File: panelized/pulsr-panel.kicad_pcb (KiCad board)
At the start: 2 copper layers, 99 x 94.5 mm, 243 parts, among them J1 JST_PH, J2 0.1" header, Q1 FDN339AN

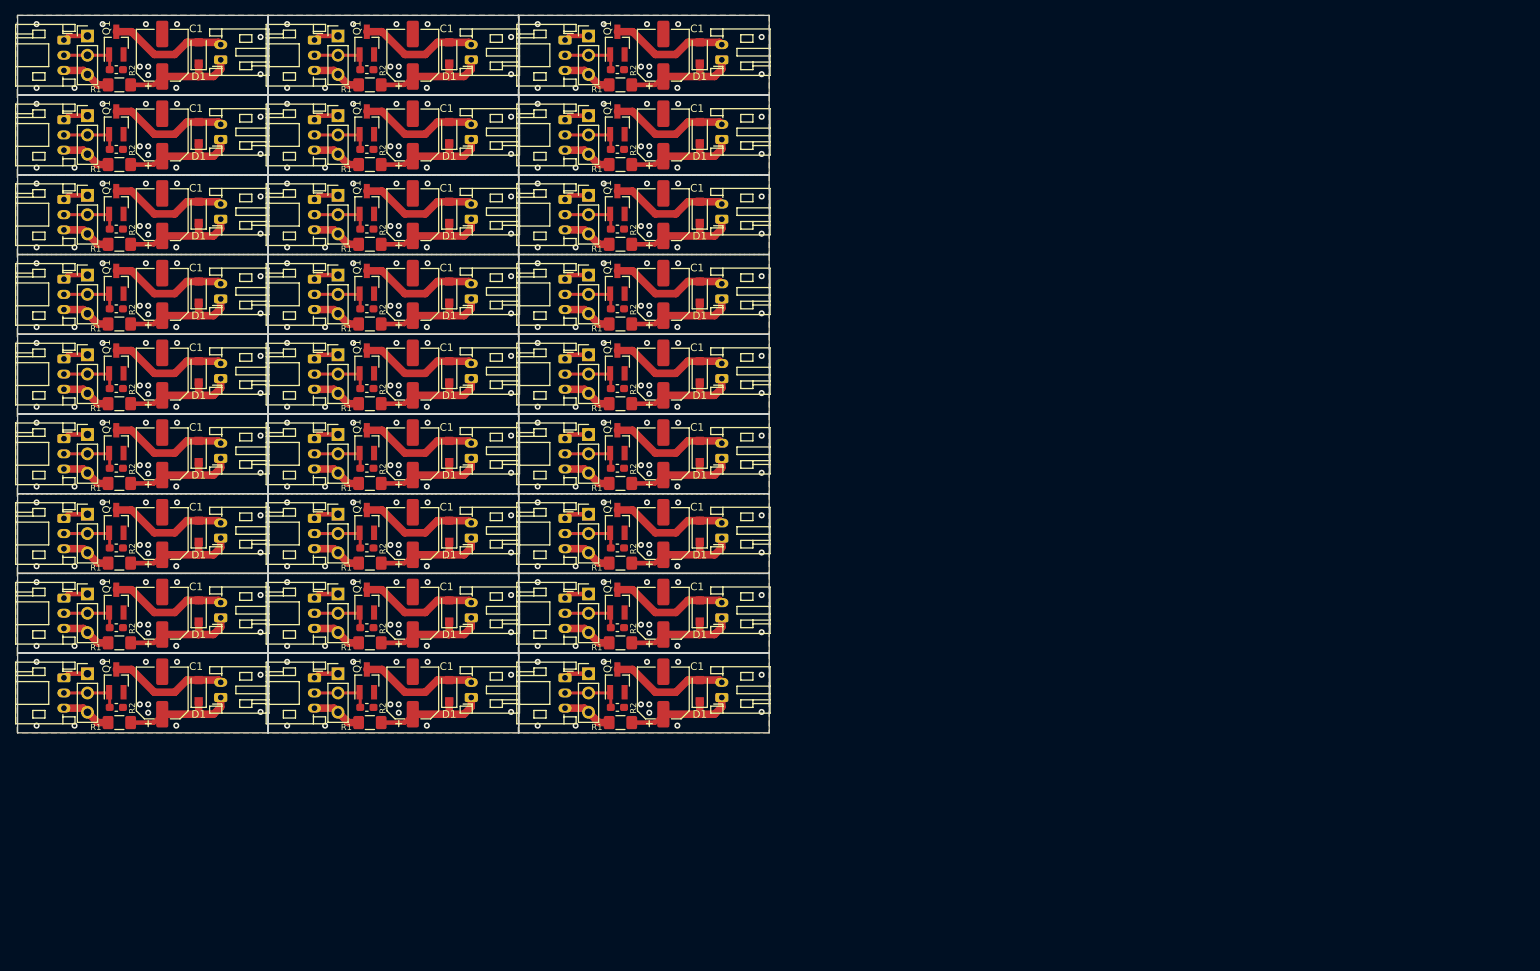
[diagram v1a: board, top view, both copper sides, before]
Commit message: Modified design to fit 47mF super-cap
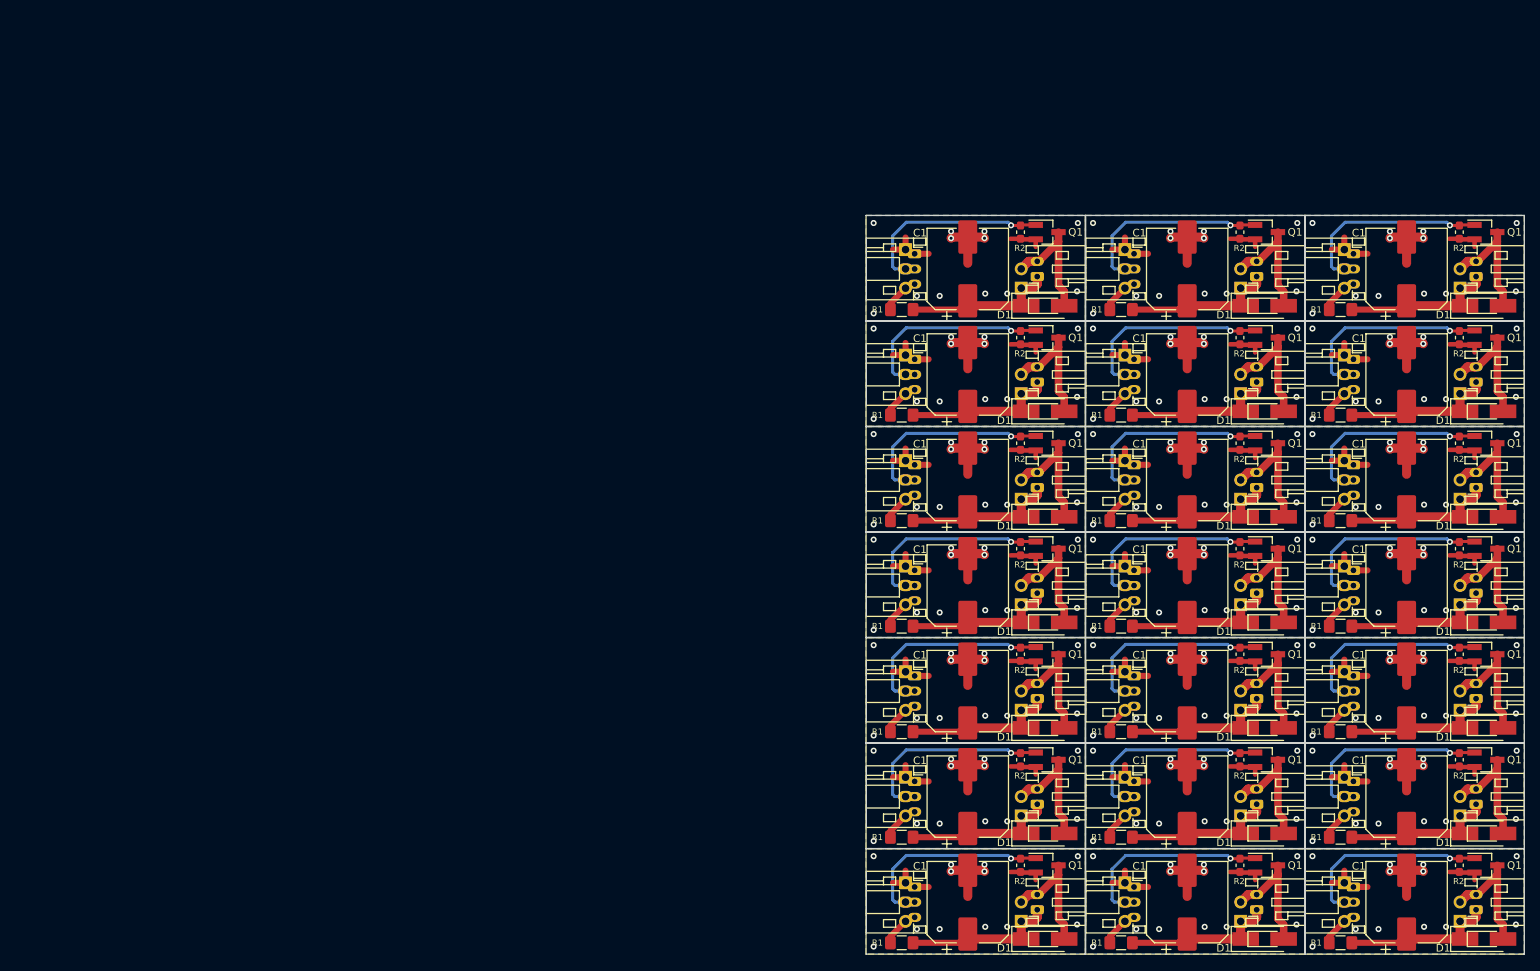
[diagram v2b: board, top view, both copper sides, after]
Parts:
- removed the C1 at (105.6, 109.6)
- removed the C1 at (105.6, 78.1)
- removed the C1 at (72.6, 78.1)
- removed the C1 at (39.6, 78.1)
- removed the C1 at (105.6, 67.6)
- removed the C1 at (72.6, 67.6)
- removed the C1 at (39.6, 67.6)
- removed the C1 at (105.6, 57.1)
- removed the C1 at (72.6, 57.1)
- removed the C1 at (39.6, 57.1)
- removed the C1 at (105.6, 46.6)
- removed the C1 at (72.6, 109.6)
- removed the C1 at (72.6, 46.6)
- removed the C1 at (39.6, 46.6)
- removed the C1 at (105.6, 36.1)
- removed the C1 at (72.6, 36.1)
- removed the C1 at (39.6, 36.1)
- removed the C1 at (105.6, 25.6)
- removed the C1 at (72.6, 25.6)
- removed the C1 at (39.6, 25.6)
- removed the C1 at (39.6, 109.6)
- removed the C1 at (105.6, 99.1)
- removed the C1 at (72.6, 99.1)
- removed the C1 at (39.6, 99.1)
- removed the C1 at (105.6, 88.6)
- removed the C1 at (72.6, 88.6)
- removed the C1 at (39.6, 88.6)
- removed the D1 at (110.4, 109.3)
- removed the D1 at (110.4, 77.8)
- removed the D1 at (77.4, 77.8)
- removed the D1 at (44.4, 77.8)
- removed the D1 at (110.4, 67.3)
- removed the D1 at (77.4, 67.3)
- removed the D1 at (44.4, 67.3)
- removed the D1 at (110.4, 56.8)
- removed the D1 at (77.4, 56.8)
- removed the D1 at (44.4, 56.8)
- removed the D1 at (110.4, 46.3)
- removed the D1 at (77.4, 109.3)
- removed the D1 at (77.4, 46.3)
- removed the D1 at (44.4, 46.3)
- removed the D1 at (110.4, 35.8)
- removed the D1 at (77.4, 35.8)
- removed the D1 at (44.4, 35.8)
- removed the D1 at (110.4, 25.3)
- removed the D1 at (77.4, 25.3)
- removed the D1 at (44.4, 109.3)
- removed the D1 at (110.4, 98.8)
- removed the D1 at (77.4, 98.8)
- removed the D1 at (44.4, 98.8)
- removed the D1 at (110.4, 88.3)
- removed the D1 at (77.4, 88.3)
- removed the D1 at (44.4, 88.3)
- removed the G*** at (104.3, 110.1)
- removed the G*** at (104.3, 78.6)
- removed the G*** at (71.3, 78.6)
- removed the G*** at (38.3, 78.6)
- removed the G*** at (104.3, 68.1)
- removed the G*** at (71.3, 68.1)
- removed the G*** at (38.3, 68.1)
- removed the G*** at (104.3, 57.6)
- removed the G*** at (71.3, 57.6)
- removed the G*** at (38.3, 57.6)
- removed the G*** at (104.3, 47.1)
- removed the G*** at (71.3, 110.1)
- removed the G*** at (71.3, 47.1)
- removed the G*** at (38.3, 47.1)
- removed the G*** at (104.3, 36.6)
- removed the G*** at (71.3, 36.6)
- removed the G*** at (38.3, 36.6)
- removed the G*** at (104.3, 26.1)
- removed the G*** at (71.3, 26.1)
- removed the G*** at (38.3, 26.1)
- removed the G*** at (38.3, 110.1)
- removed the G*** at (104.3, 99.6)
- removed the G*** at (71.3, 99.6)
- removed the G*** at (38.3, 99.6)
- removed the G*** at (104.3, 89.1)
- removed the G*** at (71.3, 89.1)
- removed the G*** at (38.3, 89.1)
- removed the J1 at (92.7, 107.6)
- removed the J1 at (92.7, 76.1)
- removed the J1 at (59.6, 76.1)
- removed the J1 at (26.6, 76.1)
- removed the J1 at (92.7, 65.6)
- removed the J1 at (59.6, 65.6)
- removed the J1 at (26.6, 65.6)
- removed the J1 at (92.7, 55.1)
- removed the J1 at (59.6, 55.1)
- removed the J1 at (26.6, 55.1)
- removed the J1 at (92.7, 44.6)
- removed the J1 at (59.6, 107.6)
- removed the J1 at (59.6, 44.6)
- removed the J1 at (26.6, 44.6)
- removed the J1 at (92.7, 34.1)
- removed the J1 at (59.6, 34.1)
- removed the J1 at (26.6, 34.1)
- removed the J1 at (92.7, 23.6)
- removed the J1 at (59.6, 23.6)
- removed the J1 at (26.6, 23.6)
- removed the J1 at (26.6, 107.6)
- removed the J1 at (92.7, 97.1)
- removed the J1 at (59.6, 97.1)
- removed the J1 at (26.6, 97.1)
- removed the J1 at (92.7, 86.6)
- removed the J1 at (59.6, 86.6)
- removed the J1 at (26.6, 86.6)
- removed the J2 at (95.8, 107.1)
- removed the J2 at (95.8, 75.6)
- removed the J2 at (62.8, 75.6)
- removed the J2 at (29.8, 75.6)
- removed the J2 at (95.8, 65.1)
- removed the J2 at (62.8, 65.1)
- removed the J2 at (29.8, 65.1)
- removed the J2 at (95.8, 54.6)
- removed the J2 at (62.8, 54.6)
- removed the J2 at (29.8, 54.6)
- removed the J2 at (95.8, 44.1)
- removed the J2 at (62.8, 107.1)
- removed the J2 at (62.8, 44.1)
- removed the J2 at (29.8, 44.1)
- removed the J2 at (95.8, 33.6)
- removed the J2 at (62.8, 33.6)
- removed the J2 at (29.8, 33.6)
- removed the J2 at (95.8, 23.1)
- removed the J2 at (62.8, 23.1)
- removed the J2 at (29.8, 107.1)
- removed the J2 at (95.8, 96.6)
- removed the J2 at (62.8, 96.6)
- removed the J2 at (29.8, 96.6)
- removed the J2 at (95.8, 86.1)
- removed the J2 at (62.8, 86.1)
- removed the J2 at (29.8, 86.1)
- removed the L1 at (113.3, 110.2)
- removed the L1 at (113.3, 78.7)
- removed the L1 at (80.3, 78.7)
- removed the L1 at (47.3, 78.7)
- removed the L1 at (113.3, 68.2)
- removed the L1 at (80.3, 68.2)
- removed the L1 at (47.3, 68.2)
- removed the L1 at (113.3, 57.7)
- removed the L1 at (80.3, 57.7)
- removed the L1 at (47.3, 57.7)
- removed the L1 at (113.3, 47.2)
- removed the L1 at (80.3, 110.2)
- removed the L1 at (80.3, 47.2)
- removed the L1 at (47.3, 47.2)
- removed the L1 at (113.3, 36.7)
- removed the L1 at (80.3, 36.7)
- removed the L1 at (47.3, 36.7)
- removed the L1 at (113.3, 26.2)
- removed the L1 at (80.3, 26.2)
- removed the L1 at (47.3, 26.2)
- removed the L1 at (47.3, 110.2)
- removed the L1 at (113.3, 99.7)
- removed the L1 at (80.3, 99.7)
- removed the L1 at (47.3, 99.7)
- removed the L1 at (113.3, 89.2)
- removed the L1 at (80.3, 89.2)
- removed the L1 at (47.3, 89.2)
- removed the Q1 at (99.5, 108.0)
- removed the Q1 at (99.5, 76.5)
- removed the Q1 at (66.5, 76.5)
- removed the Q1 at (33.5, 76.5)
- removed the Q1 at (99.5, 66.0)
- removed the Q1 at (66.5, 66.0)
- removed the Q1 at (33.5, 66.0)
- removed the Q1 at (99.5, 55.5)
- removed the Q1 at (66.5, 55.5)
- removed the Q1 at (33.5, 55.5)
- removed the Q1 at (99.5, 45.0)
- removed the Q1 at (66.5, 108.0)
- removed the Q1 at (66.5, 45.0)
- removed the Q1 at (33.5, 45.0)
- removed the Q1 at (99.5, 34.5)
- removed the Q1 at (66.5, 34.5)
- removed the Q1 at (33.5, 34.5)
- removed the Q1 at (99.5, 24.0)
- removed the Q1 at (66.5, 24.0)
- removed the Q1 at (33.5, 108.0)
- removed the Q1 at (99.5, 97.5)
- removed the Q1 at (66.5, 97.5)
- removed the Q1 at (33.5, 97.5)
- removed the Q1 at (99.5, 87.0)
- removed the Q1 at (66.5, 87.0)
- removed the Q1 at (33.5, 87.0)
- removed the R1 at (100.0, 113.5)
- removed the R1 at (100.0, 82.0)
- removed the R1 at (67.0, 82.0)
- removed the R1 at (34.0, 82.0)
- removed the R1 at (100.0, 71.5)
- removed the R1 at (67.0, 71.5)
- removed the R1 at (34.0, 71.5)
- removed the R1 at (100.0, 61.0)
- removed the R1 at (67.0, 61.0)
- removed the R1 at (34.0, 61.0)
- removed the R1 at (100.0, 50.5)
- removed the R1 at (67.0, 113.5)
- removed the R1 at (67.0, 50.5)
- removed the R1 at (34.0, 50.5)
- removed the R1 at (100.0, 40.0)
- removed the R1 at (67.0, 40.0)
- removed the R1 at (34.0, 40.0)
- removed the R1 at (100.0, 29.5)
- removed the R1 at (67.0, 29.5)
- removed the R1 at (34.0, 113.5)
- removed the R1 at (100.0, 103.0)
- removed the R1 at (67.0, 103.0)
- removed the R1 at (34.0, 103.0)
- removed the R1 at (100.0, 92.5)
- removed the R1 at (67.0, 92.5)
- removed the R1 at (34.0, 92.5)
- removed the R2 at (99.5, 111.5)
- removed the R2 at (99.5, 80.0)
- removed the R2 at (66.5, 80.0)
- removed the R2 at (33.5, 80.0)
- removed the R2 at (99.5, 69.5)
- removed the R2 at (66.5, 69.5)
- removed the R2 at (33.5, 69.5)
- removed the R2 at (99.5, 59.0)
- removed the R2 at (66.5, 59.0)
- removed the R2 at (33.5, 59.0)
- removed the R2 at (99.5, 48.5)
- removed the R2 at (66.5, 111.5)
- removed the R2 at (66.5, 48.5)
- removed the R2 at (33.5, 48.5)
- removed the R2 at (99.5, 38.0)
- removed the R2 at (66.5, 38.0)
- removed the R2 at (33.5, 38.0)
- removed the R2 at (99.5, 27.5)
- removed the R2 at (66.5, 27.5)
- removed the R2 at (33.5, 111.5)
- removed the R2 at (99.5, 101.0)
- removed the R2 at (66.5, 101.0)
- removed the R2 at (33.5, 101.0)
- removed the R2 at (99.5, 90.5)
- removed the R2 at (66.5, 90.5)
- removed the R2 at (33.5, 90.5)
- added C1: FC0H473ZFTBR24, Capacitor_SMD:CP_Elec_10x10.5, F.Cu at (145.7, 53.8)
- added C1: FC0H473ZFTBR24, Capacitor_SMD:CP_Elec_10x10.5, F.Cu at (145.7, 95.5)
- added C1: FC0H473ZFTBR24, Capacitor_SMD:CP_Elec_10x10.5, F.Cu at (174.6, 95.5)
- added C1: FC0H473ZFTBR24, Capacitor_SMD:CP_Elec_10x10.5, F.Cu at (203.5, 95.5)
- added C1: FC0H473ZFTBR24, Capacitor_SMD:CP_Elec_10x10.5, F.Cu at (145.7, 109.3)
- added C1: FC0H473ZFTBR24, Capacitor_SMD:CP_Elec_10x10.5, F.Cu at (174.6, 109.3)
- added C1: FC0H473ZFTBR24, Capacitor_SMD:CP_Elec_10x10.5, F.Cu at (203.5, 109.3)
- added C1: FC0H473ZFTBR24, Capacitor_SMD:CP_Elec_10x10.5, F.Cu at (145.7, 123.2)
- added C1: FC0H473ZFTBR24, Capacitor_SMD:CP_Elec_10x10.5, F.Cu at (174.6, 123.2)
- added C1: FC0H473ZFTBR24, Capacitor_SMD:CP_Elec_10x10.5, F.Cu at (203.5, 123.2)
- added C1: FC0H473ZFTBR24, Capacitor_SMD:CP_Elec_10x10.5, F.Cu at (145.7, 137.2)
- added C1: FC0H473ZFTBR24, Capacitor_SMD:CP_Elec_10x10.5, F.Cu at (174.6, 53.8)
- added C1: FC0H473ZFTBR24, Capacitor_SMD:CP_Elec_10x10.5, F.Cu at (174.6, 137.2)
- added C1: FC0H473ZFTBR24, Capacitor_SMD:CP_Elec_10x10.5, F.Cu at (203.5, 137.2)
- added C1: FC0H473ZFTBR24, Capacitor_SMD:CP_Elec_10x10.5, F.Cu at (203.5, 53.8)
- added C1: FC0H473ZFTBR24, Capacitor_SMD:CP_Elec_10x10.5, F.Cu at (145.7, 67.7)
- added C1: FC0H473ZFTBR24, Capacitor_SMD:CP_Elec_10x10.5, F.Cu at (174.6, 67.7)
- added C1: FC0H473ZFTBR24, Capacitor_SMD:CP_Elec_10x10.5, F.Cu at (203.5, 67.7)
- added C1: FC0H473ZFTBR24, Capacitor_SMD:CP_Elec_10x10.5, F.Cu at (145.7, 81.5)
- added C1: FC0H473ZFTBR24, Capacitor_SMD:CP_Elec_10x10.5, F.Cu at (174.6, 81.5)
- added C1: FC0H473ZFTBR24, Capacitor_SMD:CP_Elec_10x10.5, F.Cu at (203.5, 81.5)
- added D1: 1N4007L, Diode_SMD:D_SOD-123F, F.Cu at (155.9, 58.6)
- added D1: 1N4007L, Diode_SMD:D_SOD-123F, F.Cu at (155.9, 100.3)
- added D1: 1N4007L, Diode_SMD:D_SOD-123F, F.Cu at (184.8, 100.3)
- added D1: 1N4007L, Diode_SMD:D_SOD-123F, F.Cu at (213.7, 100.3)
- added D1: 1N4007L, Diode_SMD:D_SOD-123F, F.Cu at (155.9, 114.2)
- added D1: 1N4007L, Diode_SMD:D_SOD-123F, F.Cu at (184.8, 114.2)
- added D1: 1N4007L, Diode_SMD:D_SOD-123F, F.Cu at (213.7, 114.2)
- added D1: 1N4007L, Diode_SMD:D_SOD-123F, F.Cu at (155.9, 128.1)
- added D1: 1N4007L, Diode_SMD:D_SOD-123F, F.Cu at (184.8, 128.1)
- added D1: 1N4007L, Diode_SMD:D_SOD-123F, F.Cu at (213.7, 128.1)
- added D1: 1N4007L, Diode_SMD:D_SOD-123F, F.Cu at (155.9, 142.0)
- added D1: 1N4007L, Diode_SMD:D_SOD-123F, F.Cu at (184.8, 58.6)
- added D1: 1N4007L, Diode_SMD:D_SOD-123F, F.Cu at (184.8, 142.0)
- added D1: 1N4007L, Diode_SMD:D_SMA_Handsoldering, F.Cu at (155.9, 58.6)
- added D1: 1N4007L, Diode_SMD:D_SMA_Handsoldering, F.Cu at (184.8, 58.6)
- added D1: 1N4007L, Diode_SMD:D_SMA_Handsoldering, F.Cu at (213.7, 58.6)
- added D1: 1N4007L, Diode_SMD:D_SMA_Handsoldering, F.Cu at (155.9, 72.5)
- added D1: 1N4007L, Diode_SMD:D_SMA_Handsoldering, F.Cu at (184.8, 72.5)
- added D1: 1N4007L, Diode_SMD:D_SMA_Handsoldering, F.Cu at (213.7, 72.5)
- added D1: 1N4007L, Diode_SMD:D_SMA_Handsoldering, F.Cu at (155.9, 86.4)
- added D1: 1N4007L, Diode_SMD:D_SMA_Handsoldering, F.Cu at (184.8, 86.4)
- added D1: 1N4007L, Diode_SMD:D_SMA_Handsoldering, F.Cu at (213.7, 86.4)
- added D1: 1N4007L, Diode_SMD:D_SOD-123F, F.Cu at (213.7, 58.6)
- added D1: 1N4007L, Diode_SMD:D_SMA_Handsoldering, F.Cu at (155.9, 100.3)
- added D1: 1N4007L, Diode_SMD:D_SMA_Handsoldering, F.Cu at (184.8, 100.3)
- added D1: 1N4007L, Diode_SMD:D_SMA_Handsoldering, F.Cu at (213.7, 100.3)
- added D1: 1N4007L, Diode_SMD:D_SMA_Handsoldering, F.Cu at (155.9, 114.2)
- added D1: 1N4007L, Diode_SMD:D_SMA_Handsoldering, F.Cu at (184.8, 114.2)
- added D1: 1N4007L, Diode_SMD:D_SMA_Handsoldering, F.Cu at (213.7, 114.2)
- added D1: 1N4007L, Diode_SMD:D_SMA_Handsoldering, F.Cu at (155.9, 128.1)
- added D1: 1N4007L, Diode_SMD:D_SMA_Handsoldering, F.Cu at (184.8, 128.1)
- added D1: 1N4007L, Diode_SMD:D_SMA_Handsoldering, F.Cu at (213.7, 128.1)
- added D1: 1N4007L, Diode_SMD:D_SMA_Handsoldering, F.Cu at (155.9, 142.0)
- added D1: 1N4007L, Diode_SMD:D_SOD-123F, F.Cu at (155.9, 72.5)
- added D1: 1N4007L, Diode_SMD:D_SMA_Handsoldering, F.Cu at (184.8, 142.0)
- added D1: 1N4007L, Diode_SMD:D_SMA_Handsoldering, F.Cu at (213.7, 142.0)
- added D1: 1N4007L, Diode_SMD:D_SOD-123F, F.Cu at (184.8, 72.5)
- added D1: 1N4007L, Diode_SMD:D_SOD-123F, F.Cu at (213.7, 72.5)
- added D1: 1N4007L, Diode_SMD:D_SOD-123F, F.Cu at (155.9, 86.4)
- added D1: 1N4007L, Diode_SMD:D_SOD-123F, F.Cu at (184.8, 86.4)
- added D1: 1N4007L, Diode_SMD:D_SOD-123F, F.Cu at (213.7, 86.4)
- added G***: LOGO, graphics:kiwi10mm, B.Cu at (145.5, 54.1)
- added G***: LOGO, graphics:kiwi10mm, B.Cu at (145.5, 95.8)
- added G***: LOGO, graphics:kiwi10mm, B.Cu at (174.4, 95.8)
- added G***: LOGO, graphics:kiwi10mm, B.Cu at (203.3, 95.8)
- added G***: LOGO, graphics:kiwi10mm, B.Cu at (145.5, 109.7)
- added G***: LOGO, graphics:kiwi10mm, B.Cu at (174.4, 109.7)
- added G***: LOGO, graphics:kiwi10mm, B.Cu at (203.3, 109.7)
- added G***: LOGO, graphics:kiwi10mm, B.Cu at (145.5, 123.6)
- added G***: LOGO, graphics:kiwi10mm, B.Cu at (174.4, 123.6)
- added G***: LOGO, graphics:kiwi10mm, B.Cu at (203.3, 123.6)
- added G***: LOGO, graphics:kiwi10mm, B.Cu at (145.5, 137.5)
- added G***: LOGO, graphics:kiwi10mm, B.Cu at (174.4, 54.1)
- added G***: LOGO, graphics:kiwi10mm, B.Cu at (174.4, 137.5)
- added G***: LOGO, graphics:kiwi10mm, B.Cu at (203.3, 137.5)
- added G***: LOGO, graphics:kiwi10mm, B.Cu at (203.3, 54.1)
- added G***: LOGO, graphics:kiwi10mm, B.Cu at (145.5, 68.0)
- added G***: LOGO, graphics:kiwi10mm, B.Cu at (174.4, 68.0)
- added G***: LOGO, graphics:kiwi10mm, B.Cu at (203.3, 68.0)
- added G***: LOGO, graphics:kiwi10mm, B.Cu at (145.5, 81.9)
- added G***: LOGO, graphics:kiwi10mm, B.Cu at (174.4, 81.9)
- added G***: LOGO, graphics:kiwi10mm, B.Cu at (203.3, 81.9)
- added J1: JST_PH, Connector_JST:JST_PH_S3B-PH-K_1x03_P2.00mm_Horizontal, F.Cu at (138.7, 51.8)
- added J1: JST_PH, Connector_JST:JST_PH_S3B-PH-K_1x03_P2.00mm_Horizontal, F.Cu at (138.7, 93.5)
- added J1: JST_PH, Connector_JST:JST_PH_S3B-PH-K_1x03_P2.00mm_Horizontal, F.Cu at (167.6, 93.5)
- added J1: JST_PH, Connector_JST:JST_PH_S3B-PH-K_1x03_P2.00mm_Horizontal, F.Cu at (196.5, 93.5)
- added J1: JST_PH, Connector_JST:JST_PH_S3B-PH-K_1x03_P2.00mm_Horizontal, F.Cu at (138.7, 107.3)
- added J1: JST_PH, Connector_JST:JST_PH_S3B-PH-K_1x03_P2.00mm_Horizontal, F.Cu at (167.6, 107.3)
- added J1: JST_PH, Connector_JST:JST_PH_S3B-PH-K_1x03_P2.00mm_Horizontal, F.Cu at (196.5, 107.3)
- added J1: JST_PH, Connector_JST:JST_PH_S3B-PH-K_1x03_P2.00mm_Horizontal, F.Cu at (138.7, 121.2)
- added J1: JST_PH, Connector_JST:JST_PH_S3B-PH-K_1x03_P2.00mm_Horizontal, F.Cu at (167.6, 121.2)
- added J1: JST_PH, Connector_JST:JST_PH_S3B-PH-K_1x03_P2.00mm_Horizontal, F.Cu at (196.5, 121.2)
- added J1: JST_PH, Connector_JST:JST_PH_S3B-PH-K_1x03_P2.00mm_Horizontal, F.Cu at (138.7, 135.2)
- added J1: JST_PH, Connector_JST:JST_PH_S3B-PH-K_1x03_P2.00mm_Horizontal, F.Cu at (167.6, 51.8)
- added J1: JST_PH, Connector_JST:JST_PH_S3B-PH-K_1x03_P2.00mm_Horizontal, F.Cu at (167.6, 135.2)
- added J1: JST_PH, Connector_JST:JST_PH_S3B-PH-K_1x03_P2.00mm_Horizontal, F.Cu at (196.5, 135.2)
- added J1: JST_PH, Connector_JST:JST_PH_S3B-PH-K_1x03_P2.00mm_Horizontal, F.Cu at (196.5, 51.8)
- added J1: JST_PH, Connector_JST:JST_PH_S3B-PH-K_1x03_P2.00mm_Horizontal, F.Cu at (138.7, 65.7)
- added J1: JST_PH, Connector_JST:JST_PH_S3B-PH-K_1x03_P2.00mm_Horizontal, F.Cu at (167.6, 65.7)
- added J1: JST_PH, Connector_JST:JST_PH_S3B-PH-K_1x03_P2.00mm_Horizontal, F.Cu at (196.5, 65.7)
- added J1: JST_PH, Connector_JST:JST_PH_S3B-PH-K_1x03_P2.00mm_Horizontal, F.Cu at (138.7, 79.5)
- added J1: JST_PH, Connector_JST:JST_PH_S3B-PH-K_1x03_P2.00mm_Horizontal, F.Cu at (167.6, 79.5)
- added J1: JST_PH, Connector_JST:JST_PH_S3B-PH-K_1x03_P2.00mm_Horizontal, F.Cu at (196.5, 79.5)
- added J2: 0.1" header, Connector_PinHeader_2.54mm:PinHeader_1x03_P2.54mm_Vertical, F.Cu at (137.5, 51.2)
- added J2: 0.1" header, Connector_PinHeader_2.54mm:PinHeader_1x03_P2.54mm_Vertical, F.Cu at (137.5, 92.9)
- added J2: 0.1" header, Connector_PinHeader_2.54mm:PinHeader_1x03_P2.54mm_Vertical, F.Cu at (166.4, 92.9)
- added J2: 0.1" header, Connector_PinHeader_2.54mm:PinHeader_1x03_P2.54mm_Vertical, F.Cu at (195.3, 92.9)
- added J2: 0.1" header, Connector_PinHeader_2.54mm:PinHeader_1x03_P2.54mm_Vertical, F.Cu at (137.5, 106.8)
- added J2: 0.1" header, Connector_PinHeader_2.54mm:PinHeader_1x03_P2.54mm_Vertical, F.Cu at (166.4, 106.8)
- added J2: 0.1" header, Connector_PinHeader_2.54mm:PinHeader_1x03_P2.54mm_Vertical, F.Cu at (195.3, 106.8)
- added J2: 0.1" header, Connector_PinHeader_2.54mm:PinHeader_1x03_P2.54mm_Vertical, F.Cu at (137.5, 120.7)
- added J2: 0.1" header, Connector_PinHeader_2.54mm:PinHeader_1x03_P2.54mm_Vertical, F.Cu at (166.4, 120.7)
- added J2: 0.1" header, Connector_PinHeader_2.54mm:PinHeader_1x03_P2.54mm_Vertical, F.Cu at (195.3, 120.7)
- added J2: 0.1" header, Connector_PinHeader_2.54mm:PinHeader_1x03_P2.54mm_Vertical, F.Cu at (137.5, 134.6)
- added J2: 0.1" header, Connector_PinHeader_2.54mm:PinHeader_1x03_P2.54mm_Vertical, F.Cu at (166.4, 51.2)
- added J2: 0.1" header, Connector_PinHeader_2.54mm:PinHeader_1x03_P2.54mm_Vertical, F.Cu at (166.4, 134.6)
- added J2: 0.1" header, Connector_PinHeader_2.54mm:PinHeader_1x02_P2.54mm_Vertical, F.Cu at (152.7, 56.3)
- added J2: 0.1" header, Connector_PinHeader_2.54mm:PinHeader_1x02_P2.54mm_Vertical, F.Cu at (181.6, 56.3)
- added J2: 0.1" header, Connector_PinHeader_2.54mm:PinHeader_1x02_P2.54mm_Vertical, F.Cu at (210.5, 56.3)
- added J2: 0.1" header, Connector_PinHeader_2.54mm:PinHeader_1x02_P2.54mm_Vertical, F.Cu at (152.7, 70.2)
- added J2: 0.1" header, Connector_PinHeader_2.54mm:PinHeader_1x02_P2.54mm_Vertical, F.Cu at (181.6, 70.2)
- added J2: 0.1" header, Connector_PinHeader_2.54mm:PinHeader_1x02_P2.54mm_Vertical, F.Cu at (210.5, 70.2)
- added J2: 0.1" header, Connector_PinHeader_2.54mm:PinHeader_1x02_P2.54mm_Vertical, F.Cu at (152.7, 84.1)
- added J2: 0.1" header, Connector_PinHeader_2.54mm:PinHeader_1x02_P2.54mm_Vertical, F.Cu at (181.6, 84.1)
- added J2: 0.1" header, Connector_PinHeader_2.54mm:PinHeader_1x02_P2.54mm_Vertical, F.Cu at (210.5, 84.1)
- added J2: 0.1" header, Connector_PinHeader_2.54mm:PinHeader_1x03_P2.54mm_Vertical, F.Cu at (195.3, 51.2)
- added J2: 0.1" header, Connector_PinHeader_2.54mm:PinHeader_1x02_P2.54mm_Vertical, F.Cu at (152.7, 98.0)
- added J2: 0.1" header, Connector_PinHeader_2.54mm:PinHeader_1x02_P2.54mm_Vertical, F.Cu at (181.6, 98.0)
- added J2: 0.1" header, Connector_PinHeader_2.54mm:PinHeader_1x02_P2.54mm_Vertical, F.Cu at (210.5, 98.0)
- added J2: 0.1" header, Connector_PinHeader_2.54mm:PinHeader_1x02_P2.54mm_Vertical, F.Cu at (152.7, 111.9)
- added J2: 0.1" header, Connector_PinHeader_2.54mm:PinHeader_1x02_P2.54mm_Vertical, F.Cu at (181.6, 111.9)
- added J2: 0.1" header, Connector_PinHeader_2.54mm:PinHeader_1x02_P2.54mm_Vertical, F.Cu at (210.5, 111.9)
- added J2: 0.1" header, Connector_PinHeader_2.54mm:PinHeader_1x02_P2.54mm_Vertical, F.Cu at (152.7, 125.8)
- added J2: 0.1" header, Connector_PinHeader_2.54mm:PinHeader_1x02_P2.54mm_Vertical, F.Cu at (181.6, 125.8)
- added J2: 0.1" header, Connector_PinHeader_2.54mm:PinHeader_1x02_P2.54mm_Vertical, F.Cu at (210.5, 125.8)
- added J2: 0.1" header, Connector_PinHeader_2.54mm:PinHeader_1x02_P2.54mm_Vertical, F.Cu at (152.7, 139.7)
- added J2: 0.1" header, Connector_PinHeader_2.54mm:PinHeader_1x03_P2.54mm_Vertical, F.Cu at (137.5, 65.1)
- added J2: 0.1" header, Connector_PinHeader_2.54mm:PinHeader_1x02_P2.54mm_Vertical, F.Cu at (181.6, 139.7)
- added J2: 0.1" header, Connector_PinHeader_2.54mm:PinHeader_1x02_P2.54mm_Vertical, F.Cu at (210.5, 139.7)
- added J2: 0.1" header, Connector_PinHeader_2.54mm:PinHeader_1x03_P2.54mm_Vertical, F.Cu at (166.4, 65.1)
- added J2: 0.1" header, Connector_PinHeader_2.54mm:PinHeader_1x03_P2.54mm_Vertical, F.Cu at (195.3, 65.1)
- added J2: 0.1" header, Connector_PinHeader_2.54mm:PinHeader_1x03_P2.54mm_Vertical, F.Cu at (137.5, 79.0)
- added J2: 0.1" header, Connector_PinHeader_2.54mm:PinHeader_1x03_P2.54mm_Vertical, F.Cu at (166.4, 79.0)
- added J2: 0.1" header, Connector_PinHeader_2.54mm:PinHeader_1x03_P2.54mm_Vertical, F.Cu at (195.3, 79.0)
- added L1: solenoid, Connector_JST:JST_PH_S2B-PH-K_1x02_P2.00mm_Horizontal, F.Cu at (154.8, 54.8)
- added L1: solenoid, Connector_JST:JST_PH_S2B-PH-K_1x02_P2.00mm_Horizontal, F.Cu at (154.8, 96.5)
- added L1: solenoid, Connector_JST:JST_PH_S2B-PH-K_1x02_P2.00mm_Horizontal, F.Cu at (183.8, 96.5)
- added L1: solenoid, Connector_JST:JST_PH_S2B-PH-K_1x02_P2.00mm_Horizontal, F.Cu at (212.7, 96.5)
- added L1: solenoid, Connector_JST:JST_PH_S2B-PH-K_1x02_P2.00mm_Horizontal, F.Cu at (154.8, 110.3)
- added L1: solenoid, Connector_JST:JST_PH_S2B-PH-K_1x02_P2.00mm_Horizontal, F.Cu at (183.8, 110.3)
- added L1: solenoid, Connector_JST:JST_PH_S2B-PH-K_1x02_P2.00mm_Horizontal, F.Cu at (212.7, 110.3)
- added L1: solenoid, Connector_JST:JST_PH_S2B-PH-K_1x02_P2.00mm_Horizontal, F.Cu at (154.8, 124.2)
- added L1: solenoid, Connector_JST:JST_PH_S2B-PH-K_1x02_P2.00mm_Horizontal, F.Cu at (183.8, 124.2)
- added L1: solenoid, Connector_JST:JST_PH_S2B-PH-K_1x02_P2.00mm_Horizontal, F.Cu at (212.7, 124.2)
- added L1: solenoid, Connector_JST:JST_PH_S2B-PH-K_1x02_P2.00mm_Horizontal, F.Cu at (154.8, 138.2)
- added L1: solenoid, Connector_JST:JST_PH_S2B-PH-K_1x02_P2.00mm_Horizontal, F.Cu at (183.8, 54.8)
- added L1: solenoid, Connector_JST:JST_PH_S2B-PH-K_1x02_P2.00mm_Horizontal, F.Cu at (183.8, 138.2)
- added L1: solenoid, Connector_JST:JST_PH_S2B-PH-K_1x02_P2.00mm_Horizontal, F.Cu at (212.7, 138.2)
- added L1: solenoid, Connector_JST:JST_PH_S2B-PH-K_1x02_P2.00mm_Horizontal, F.Cu at (212.7, 54.8)
- added L1: solenoid, Connector_JST:JST_PH_S2B-PH-K_1x02_P2.00mm_Horizontal, F.Cu at (154.8, 68.7)
- added L1: solenoid, Connector_JST:JST_PH_S2B-PH-K_1x02_P2.00mm_Horizontal, F.Cu at (183.8, 68.7)
- added L1: solenoid, Connector_JST:JST_PH_S2B-PH-K_1x02_P2.00mm_Horizontal, F.Cu at (212.7, 68.7)
- added L1: solenoid, Connector_JST:JST_PH_S2B-PH-K_1x02_P2.00mm_Horizontal, F.Cu at (154.8, 82.5)
- added L1: solenoid, Connector_JST:JST_PH_S2B-PH-K_1x02_P2.00mm_Horizontal, F.Cu at (183.8, 82.5)
- added L1: solenoid, Connector_JST:JST_PH_S2B-PH-K_1x02_P2.00mm_Horizontal, F.Cu at (212.7, 82.5)
- added Q1: FDN339AN, Package_TO_SOT_SMD:SOT-23_Handsoldering, F.Cu at (156.2, 48.9)
- added Q1: FDN339AN, Package_TO_SOT_SMD:SOT-23_Handsoldering, F.Cu at (156.2, 90.6)
- added Q1: FDN339AN, Package_TO_SOT_SMD:SOT-23_Handsoldering, F.Cu at (185.1, 90.6)
- added Q1: FDN339AN, Package_TO_SOT_SMD:SOT-23_Handsoldering, F.Cu at (213.9, 90.6)
- added Q1: FDN339AN, Package_TO_SOT_SMD:SOT-23_Handsoldering, F.Cu at (156.2, 104.5)
- added Q1: FDN339AN, Package_TO_SOT_SMD:SOT-23_Handsoldering, F.Cu at (185.1, 104.5)
- added Q1: FDN339AN, Package_TO_SOT_SMD:SOT-23_Handsoldering, F.Cu at (213.9, 104.5)
- added Q1: FDN339AN, Package_TO_SOT_SMD:SOT-23_Handsoldering, F.Cu at (156.2, 118.4)
- added Q1: FDN339AN, Package_TO_SOT_SMD:SOT-23_Handsoldering, F.Cu at (185.1, 118.4)
- added Q1: FDN339AN, Package_TO_SOT_SMD:SOT-23_Handsoldering, F.Cu at (213.9, 118.4)
- added Q1: FDN339AN, Package_TO_SOT_SMD:SOT-23_Handsoldering, F.Cu at (156.2, 132.3)
- added Q1: FDN339AN, Package_TO_SOT_SMD:SOT-23_Handsoldering, F.Cu at (185.1, 48.9)
- added Q1: FDN339AN, Package_TO_SOT_SMD:SOT-23_Handsoldering, F.Cu at (185.1, 132.3)
- added Q1: FDN339AN, Package_TO_SOT_SMD:SOT-23_Handsoldering, F.Cu at (213.9, 48.9)
- added Q1: FDN339AN, Package_TO_SOT_SMD:SOT-23_Handsoldering, F.Cu at (156.2, 62.8)
- added Q1: FDN339AN, Package_TO_SOT_SMD:SOT-23_Handsoldering, F.Cu at (185.1, 62.8)
- added Q1: FDN339AN, Package_TO_SOT_SMD:SOT-23_Handsoldering, F.Cu at (213.9, 62.8)
- added Q1: FDN339AN, Package_TO_SOT_SMD:SOT-23_Handsoldering, F.Cu at (156.2, 76.7)
- added Q1: FDN339AN, Package_TO_SOT_SMD:SOT-23_Handsoldering, F.Cu at (185.1, 76.7)
- added Q1: FDN339AN, Package_TO_SOT_SMD:SOT-23_Handsoldering, F.Cu at (213.9, 76.7)
- added R1: 22R, Resistor_SMD:R_1206_3216Metric_Pad1.42x1.75mm_HandSolder, F.Cu at (137.0, 59.1)
- added R1: 22R, Resistor_SMD:R_1206_3216Metric_Pad1.42x1.75mm_HandSolder, F.Cu at (137.0, 100.8)
- added R1: 22R, Resistor_SMD:R_1206_3216Metric_Pad1.42x1.75mm_HandSolder, F.Cu at (165.9, 100.8)
- added R1: 22R, Resistor_SMD:R_1206_3216Metric_Pad1.42x1.75mm_HandSolder, F.Cu at (194.8, 100.8)
- added R1: 22R, Resistor_SMD:R_1206_3216Metric_Pad1.42x1.75mm_HandSolder, F.Cu at (137.0, 114.7)
- added R1: 22R, Resistor_SMD:R_1206_3216Metric_Pad1.42x1.75mm_HandSolder, F.Cu at (165.9, 114.7)
- added R1: 22R, Resistor_SMD:R_1206_3216Metric_Pad1.42x1.75mm_HandSolder, F.Cu at (194.8, 114.7)
- added R1: 22R, Resistor_SMD:R_1206_3216Metric_Pad1.42x1.75mm_HandSolder, F.Cu at (137.0, 128.6)
- added R1: 22R, Resistor_SMD:R_1206_3216Metric_Pad1.42x1.75mm_HandSolder, F.Cu at (165.9, 128.6)
- added R1: 22R, Resistor_SMD:R_1206_3216Metric_Pad1.42x1.75mm_HandSolder, F.Cu at (194.8, 128.6)
- added R1: 22R, Resistor_SMD:R_1206_3216Metric_Pad1.42x1.75mm_HandSolder, F.Cu at (137.0, 142.5)
- added R1: 22R, Resistor_SMD:R_1206_3216Metric_Pad1.42x1.75mm_HandSolder, F.Cu at (165.9, 59.1)
- added R1: 22R, Resistor_SMD:R_1206_3216Metric_Pad1.42x1.75mm_HandSolder, F.Cu at (165.9, 142.5)
- added R1: 22R, Resistor_SMD:R_1206_3216Metric_Pad1.42x1.75mm_HandSolder, F.Cu at (194.8, 59.1)
- added R1: 22R, Resistor_SMD:R_1206_3216Metric_Pad1.42x1.75mm_HandSolder, F.Cu at (137.0, 73.0)
- added R1: 22R, Resistor_SMD:R_1206_3216Metric_Pad1.42x1.75mm_HandSolder, F.Cu at (165.9, 73.0)
- added R1: 22R, Resistor_SMD:R_1206_3216Metric_Pad1.42x1.75mm_HandSolder, F.Cu at (194.8, 73.0)
- added R1: 22R, Resistor_SMD:R_1206_3216Metric_Pad1.42x1.75mm_HandSolder, F.Cu at (137.0, 86.9)
- added R1: 22R, Resistor_SMD:R_1206_3216Metric_Pad1.42x1.75mm_HandSolder, F.Cu at (165.9, 86.9)
- added R1: 22R, Resistor_SMD:R_1206_3216Metric_Pad1.42x1.75mm_HandSolder, F.Cu at (194.8, 86.9)
- added R2: 10k, Resistor_SMD:R_0603_1608Metric_Pad1.05x0.95mm_HandSolder, F.Cu at (152.7, 48.9)
- added R2: 10k, Resistor_SMD:R_0603_1608Metric_Pad1.05x0.95mm_HandSolder, F.Cu at (152.7, 90.6)
- added R2: 10k, Resistor_SMD:R_0603_1608Metric_Pad1.05x0.95mm_HandSolder, F.Cu at (181.6, 90.6)
- added R2: 10k, Resistor_SMD:R_0603_1608Metric_Pad1.05x0.95mm_HandSolder, F.Cu at (210.4, 90.6)
- added R2: 10k, Resistor_SMD:R_0603_1608Metric_Pad1.05x0.95mm_HandSolder, F.Cu at (152.7, 104.5)
- added R2: 10k, Resistor_SMD:R_0603_1608Metric_Pad1.05x0.95mm_HandSolder, F.Cu at (181.6, 104.5)
- added R2: 10k, Resistor_SMD:R_0603_1608Metric_Pad1.05x0.95mm_HandSolder, F.Cu at (210.4, 104.5)
- added R2: 10k, Resistor_SMD:R_0603_1608Metric_Pad1.05x0.95mm_HandSolder, F.Cu at (152.7, 118.4)
- added R2: 10k, Resistor_SMD:R_0603_1608Metric_Pad1.05x0.95mm_HandSolder, F.Cu at (181.6, 118.4)
- added R2: 10k, Resistor_SMD:R_0603_1608Metric_Pad1.05x0.95mm_HandSolder, F.Cu at (210.4, 118.4)
- added R2: 10k, Resistor_SMD:R_0603_1608Metric_Pad1.05x0.95mm_HandSolder, F.Cu at (152.7, 132.3)
- added R2: 10k, Resistor_SMD:R_0603_1608Metric_Pad1.05x0.95mm_HandSolder, F.Cu at (181.6, 48.9)
- added R2: 10k, Resistor_SMD:R_0603_1608Metric_Pad1.05x0.95mm_HandSolder, F.Cu at (181.6, 132.3)
- added R2: 10k, Resistor_SMD:R_0603_1608Metric_Pad1.05x0.95mm_HandSolder, F.Cu at (210.4, 48.9)
- added R2: 10k, Resistor_SMD:R_0603_1608Metric_Pad1.05x0.95mm_HandSolder, F.Cu at (152.7, 62.8)
- added R2: 10k, Resistor_SMD:R_0603_1608Metric_Pad1.05x0.95mm_HandSolder, F.Cu at (181.6, 62.8)
- added R2: 10k, Resistor_SMD:R_0603_1608Metric_Pad1.05x0.95mm_HandSolder, F.Cu at (210.4, 62.8)
- added R2: 10k, Resistor_SMD:R_0603_1608Metric_Pad1.05x0.95mm_HandSolder, F.Cu at (152.7, 76.7)
- added R2: 10k, Resistor_SMD:R_0603_1608Metric_Pad1.05x0.95mm_HandSolder, F.Cu at (181.6, 76.7)
- added R2: 10k, Resistor_SMD:R_0603_1608Metric_Pad1.05x0.95mm_HandSolder, F.Cu at (210.4, 76.7)
- moved Q1 210.4 mm to (213.9, 132.3), turned to 0 degrees
- moved D1 205.6 mm to (213.7, 142.0), turned to 0 degrees
- moved R2 205.6 mm to (210.4, 132.3), turned to 90 degrees
- moved J2 199.6 mm to (195.3, 134.6)
- moved R1 196.6 mm to (194.8, 142.5)
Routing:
- net /FIRE!: track 216.6 -> 564.3 mm, vias 0 -> 21
- net GND: track 89.7 -> 419.3 mm, vias 324 -> 252
- net +5V: track 178.2 -> 104.2 mm
- net Net-(D1-Pad2): track 426.1 -> 363.5 mm
- net Net-(C1-Pad1): track 423.4 -> 476.3 mm
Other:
- board size 99 x 94.5 mm -> 86.7 x 97.3 mm
- board text added: "5V"
- board text added: "FIRE!"
- board text added: "GND"
- board text added: "Pulsr"
- board text added: "v1.1.0"
- board text removed: "5V FIRE! GND"
- board text removed: "v1.0.1"
